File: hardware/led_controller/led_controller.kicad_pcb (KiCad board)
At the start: 2 copper layers, 65 x 50 mm, 38 parts, among them J1 Barrel_Jack_Switch, J2 Conn_01x06, J3 Conn_01x04, J4 Screw_Terminal_01x04, Q1 BC807, Q2 IRLML0030TRPBF-1, Q3 BC807, Q4 IRLML0030TRPBF-1, Q5 BC807, Q6 IRLML0030TRPBF-1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

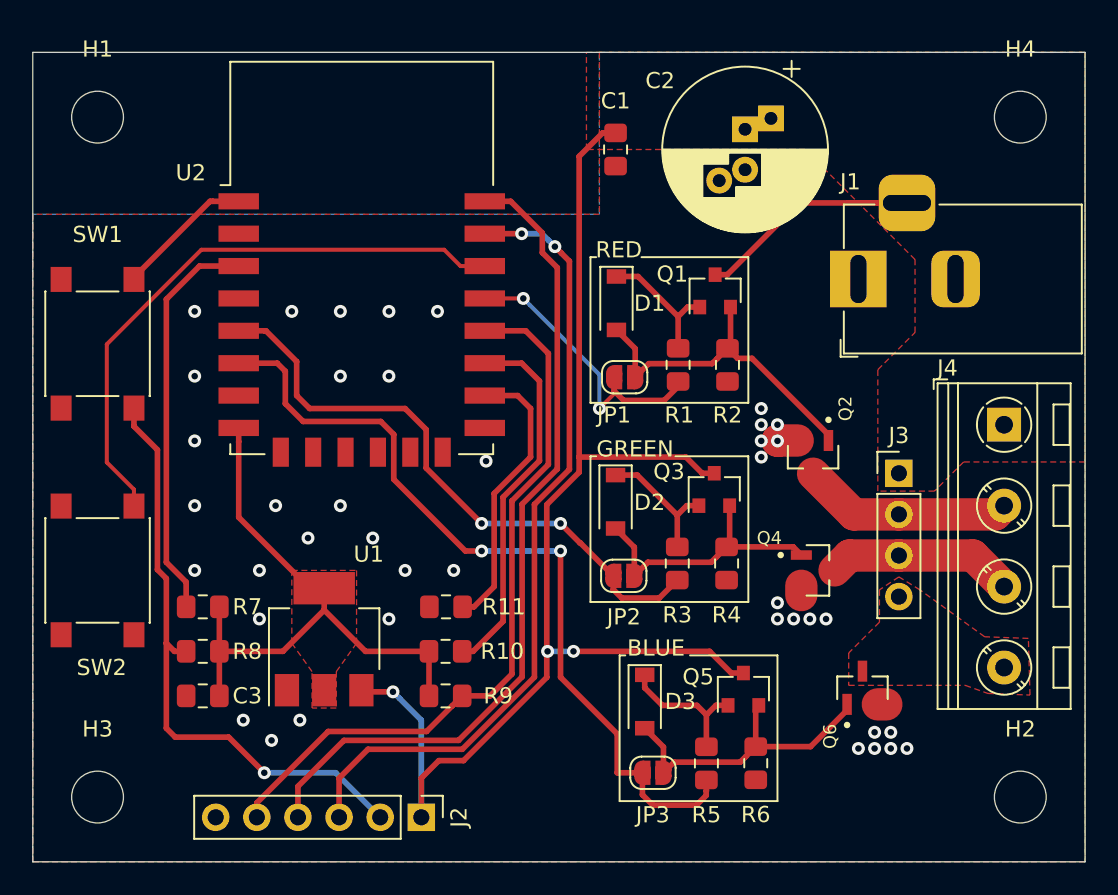
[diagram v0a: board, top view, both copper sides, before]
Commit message: Removed bakers clamps. reduced board size to 55x50 mm
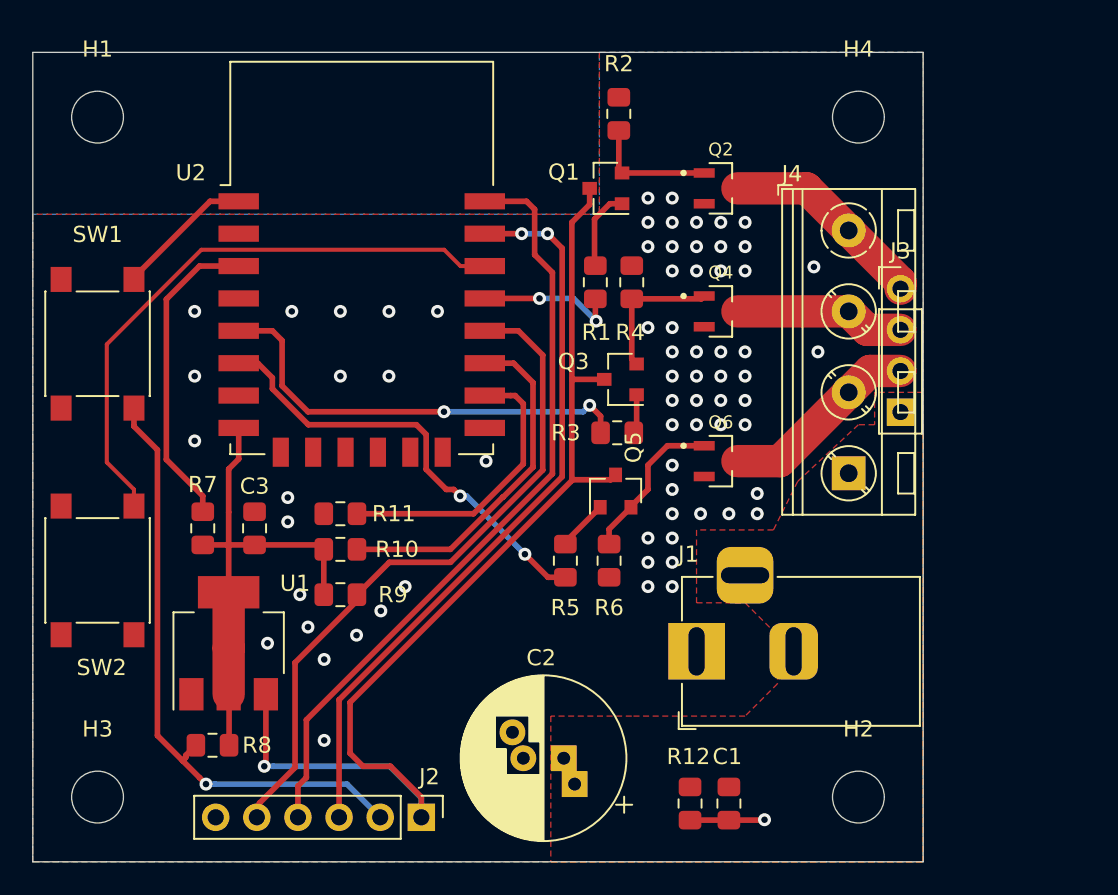
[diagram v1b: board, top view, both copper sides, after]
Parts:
- removed D1, D2, D3: 1N4148W, Diode_SMD:D_SOD-123
- removed JP1: Red, Jumper:SolderJumper-2_P1.3mm_Open_RoundedPad1.0x1.5mm
- removed JP2: Green, Jumper:SolderJumper-2_P1.3mm_Open_RoundedPad1.0x1.5mm
- removed JP3: Blue, Jumper:SolderJumper-2_P1.3mm_Open_RoundedPad1.0x1.5mm
- added R12: 100K, Resistor_SMD:R_0805_2012Metric_Pad1.15x1.40mm_HandSolder, F.Cu at (40.6, 46.4)
- moved C1 41.0 mm to (43.0, 46.4)
- moved C2 40.4 mm to (32.8, 43.6), turned to 180 degrees
- moved J1 25.1 mm to (41.0, 37.0)
- moved R4 18.3 mm to (37.0, 14.2), turned to 90 degrees
- moved Q2 17.6 mm to (42.5, 8.40), turned to 0 degrees
- moved Q4 17.1 mm to (42.5, 16.0)
- moved R2 16.9 mm to (36.2, 3.80), turned to 90 degrees
- moved Q6 16.5 mm to (42.5, 25.2), turned to 0 degrees
- moved R6 15.4 mm to (35.6, 31.4)
- moved J4 15.4 mm to (50.4, 11.0)
- moved R5 15.3 mm to (32.9, 31.4)
- moved Q5 14.6 mm to (36.0, 27.1)
- moved J3 11.4 mm to (53.6, 14.6)
- moved C3 10.8 mm to (13.7, 29.4), turned to 90 degrees
- moved H2 10.0 mm to (51.0, 46.0)
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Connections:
- J3 pad 1: +12V -> /DRAIN_RED
- J3 pad 2: /DRAIN_RED -> /DRAIN_GREEN
- J3 pad 3: /DRAIN_GREEN -> /DRAIN_BLUE
- J3 pad 4: /DRAIN_BLUE -> +12V
- J4 pad 1: +12V -> /DRAIN_RED
- J4 pad 2: /DRAIN_RED -> /DRAIN_GREEN
- J4 pad 3: /DRAIN_GREEN -> /DRAIN_BLUE
- J4 pad 4: /DRAIN_BLUE -> +12V
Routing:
- net +12V: track 98.1 -> 68.8 mm, vias 3 -> 1
- net /SIG_BLUE: track 51.0 -> 27.3 mm
- net Net-(Q1-Pad2): track 21.3 -> 7.78 mm
- net /DRAIN_BLUE: track 0.00 -> 12.4 mm
- net /SIG_RED: track 19.1 -> 8.86 mm
- net /SIG_GREEN: track 37.5 -> 27.5 mm
- net Net-(Q5-Pad2): track 19.2 -> 9.84 mm
- net Net-(Q3-Pad2): track 17.3 -> 8.70 mm
- net +3V3: track 37.6 -> 30.3 mm
- net Net-(Q3-Pad1): track 8.37 -> 2.42 mm
- net Net-(Q5-Pad1): track 8.85 -> 3.17 mm
- net Net-(R7-Pad1): track 24.8 -> 19.4 mm
- net /FL_TX: track 51.6 -> 47.8 mm
- net /FL_RX: track 49.6 -> 46.0 mm
- net Net-(Q1-Pad1): track 8.37 -> 4.99 mm
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- removed copper zone on F.Cu, net +3V3
- removed copper zone on F.Cu, net /DRAIN_BLUE
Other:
- board size 65 x 50 mm -> 55 x 50 mm
- board text removed: "BLUE"
- board text removed: "GREEN"
- board text removed: "RED"

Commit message: finished board design
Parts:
- added Q7: BC817, Package_TO_SOT_SMD:SOT-23, F.Cu at (22.8, 40.8)
- added Q8: BC817, Package_TO_SOT_SMD:SOT-23, F.Cu at (42.6, 4.10)
- added Q9: BC817, Package_TO_SOT_SMD:SOT-23, F.Cu at (30.9, 36.8)
- added R13: 1K, Resistor_SMD:R_0805_2012Metric_Pad1.15x1.40mm_HandSolder, F.Cu at (25.5, 46.1)
- added R14: 1K, Resistor_SMD:R_0805_2012Metric_Pad1.15x1.40mm_HandSolder, F.Cu at (37.2, 4.00)
- added R15: 1K, Resistor_SMD:R_0805_2012Metric_Pad1.15x1.40mm_HandSolder, F.Cu at (23.5, 36.7)
- added R16: 100R, Resistor_SMD:R_0805_2012Metric_Pad1.15x1.40mm_HandSolder, F.Cu at (45.6, 4.00)
- added R17: 100R, Resistor_SMD:R_0805_2012Metric_Pad1.15x1.40mm_HandSolder, F.Cu at (31.7, 32.1)
- added R18: 100R, Resistor_SMD:R_0805_2012Metric_Pad1.15x1.40mm_HandSolder, F.Cu at (29.3, 32.1)
- R2, R4, R6: value 100R -> 1K
- moved Q3 19.1 mm to (26.9, 36.8), turned to 90 degrees
- moved R5 16.5 mm to (19.2, 40.8), turned to 90 degrees
- moved Q5 16.4 mm to (26.9, 40.8), turned to 180 degrees
- moved R3 13.8 mm to (26.1, 33.0)
- moved R12 12.6 mm to (28.0, 46.1), turned to 270 degrees
- moved R1 11.4 mm to (39.8, 4.00), turned to 90 degrees
- moved R6 6.14 mm to (36.3, 25.3)
- moved R2 4.78 mm to (35.0, 8.43), turned to 270 degrees
- moved Q1 4.44 mm to (34.3, 4.10)
- moved C2 3.21 mm to (36.0, 43.8)
- moved C1 2.72 mm to (45.6, 47.2), turned to 0 degrees
- moved R4 2.55 mm to (35.3, 16.1), turned to 270 degrees
- moved J2 1.75 mm to (22.2, 47.2)
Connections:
- Q2 pad 1: Net-(Q1-Pad2) -> Net-(Q2-Pad1)
- Q4 pad 1: Net-(Q3-Pad2) -> Net-(Q4-Pad1)
- Q6 pad 1: Net-(Q5-Pad2) -> Net-(Q6-Pad1)
- R1 pad 1: Net-(Q1-Pad1) -> Net-(Q8-Pad1)
- R2 pad 1: Net-(Q1-Pad2) -> Net-(Q2-Pad1)
- R3 pad 1: Net-(Q3-Pad1) -> Net-(Q9-Pad1)
- R4 pad 1: Net-(Q3-Pad2) -> Net-(Q4-Pad1)
- R5 pad 1: Net-(Q5-Pad1) -> Net-(Q7-Pad1)
- R6 pad 1: Net-(Q5-Pad2) -> Net-(Q6-Pad1)
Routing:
- net +12V: track 68.8 -> 106.5 mm
- net Net-(Q4-Pad1): track 0.00 -> 25.2 mm
- net /SIG_RED: track 8.86 -> 24.4 mm
- net Net-(Q6-Pad1): track 0.00 -> 14.8 mm
- net Net-(Q2-Pad1): track 0.00 -> 11.6 mm
- net Net-(Q3-Pad1): track 2.42 -> 11.4 mm
- net Net-(Q5-Pad1): track 3.17 -> 9.35 mm
- net /SIG_GREEN: track 27.5 -> 22.8 mm
- net Net-(Q1-Pad2): track 7.78 -> 11.9 mm
- net /FL_RX: track 46.0 -> 50.1 mm
- net Net-(Q9-Pad1): track 0.00 -> 4.03 mm
- net Net-(Q7-Pad1): track 0.00 -> 3.92 mm
- net Net-(Q8-Pad1): track 0.00 -> 3.81 mm
- net /FL_TX: track 47.8 -> 51.3 mm
- net GND: track 4.61 -> 1.84 mm, vias 70 -> 155
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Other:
- board text added: "RESET"
- board text added: "WPS"

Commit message: Modified connectors and silkscreens. Added a diode to keep capacitor from charging during flashing. Added a second layer to mosfet connector traces and stiched them to help power dissipation.
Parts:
- removed J3: Conn_01x04, Connector_PinHeader_2.54mm:PinHeader_1x04_P2.54mm_Vertical
- added D1: 1N4148, Diode_SMD:D_SOD-123, F.Cu at (23.8, 45.5)
- J2: footprint Connector_PinHeader_2.54mm:PinHeader_1x06_P2.54mm_Vertical -> led_controller:Header_Programming
- J4: footprint TerminalBlock_RND:TerminalBlock_RND_205-00047_1x04_P5.00mm_Horizontal -> led_controller:connector_led
- moved J4 9.08 mm to (45.0, 18.3), turned to 90 degrees
- moved J2 8.00 mm to (14.2, 47.3), turned to 0 degrees
- moved Q2 2.00 mm to (40.5, 8.40)
- moved Q4 2.00 mm to (40.5, 16.0)
- moved Q6 2.00 mm to (40.5, 25.2)
- moved R13 0.56 mm to (26.1, 46.2)
- moved R12 0.33 mm to (28.3, 46.2)
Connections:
- J2 pad 1: +12V -> +12L
- J2 pad 2: /BTN_RST -> /FL_TX
- J2 pad 4: /FL_TX -> /FL_DTR
- J2 pad 5: /FL_DTR -> /BTN_RST
- U1 pad 3: +12V -> +12L
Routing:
- net +12V: track 106.5 -> 89.6 mm, vias 1 -> 0
- net +12L: track 0.00 -> 16.2 mm, vias 0 -> 1
- net /DRAIN_BLUE: track 12.4 -> 26.9 mm, vias 0 -> 5
- net /DRAIN_RED: track 12.9 -> 27.2 mm, vias 0 -> 7
- net /DRAIN_GREEN: track 10.5 -> 23.2 mm, vias 0 -> 4
- net /BTN_RST: track 45.2 -> 38.0 mm, vias 1 -> 0
- net /SIG_RED: track 24.4 -> 27.9 mm
- net Net-(Q6-Pad1): track 14.8 -> 12.8 mm
- net /FL_RX: track 50.1 -> 48.2 mm, vias 2 -> 0
- net Net-(Q4-Pad1): track 25.2 -> 23.9 mm
- net /FL_DTR: track 44.2 -> 43.4 mm
- net Net-(R11-Pad2): track 17.9 -> 17.2 mm
- net Net-(Q5-Pad1): track 9.35 -> 8.73 mm
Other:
- board text added: "12V"
- board text added: "Aurora V1, Dec. 2019 Abdullah Çanakçı github.com/abdullahcanakci/aurora"
- board text added: "B"
- board text added: "G"
- board text added: "R"
